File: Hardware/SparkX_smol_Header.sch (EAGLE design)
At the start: 31 parts, among them J1 QWIIC_RIGHT_ANGLE

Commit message: Update smôl logo
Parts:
- added U$39: SMOL_LOGOSMALL, SparkX:SMOL_LOGOSMALL
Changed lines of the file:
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@@
 <part name="LOGO3" library="SparkFun-Aesthetics" deviceset="OSHW-LOGO" device="MINI"/>
 <part name="LOGO4" library="SparkFun-Aesthetics" deviceset="QWIIC_LOGO" device="_5MM"/>
+<part name="U$39" library="SparkX" deviceset="SMOL_LOGO" device="SMALL"/>
 </parts>
 <sheets>
@@
 <instance part="LOGO3" gate="G$1" x="307.34" y="25.4" smashed="yes"/>
 <instance part="LOGO4" gate="G$1" x="307.34" y="38.1" smashed="yes"/>
+<instance part="U$39" gate="G$1" x="307.34" y="50.8" smashed="yes"/>
 </instances>
 <busses>

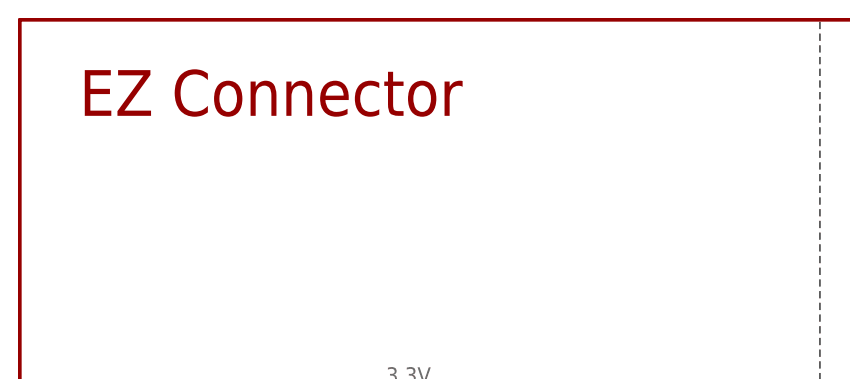
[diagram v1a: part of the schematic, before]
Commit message: Change EZ to smôl on schematic
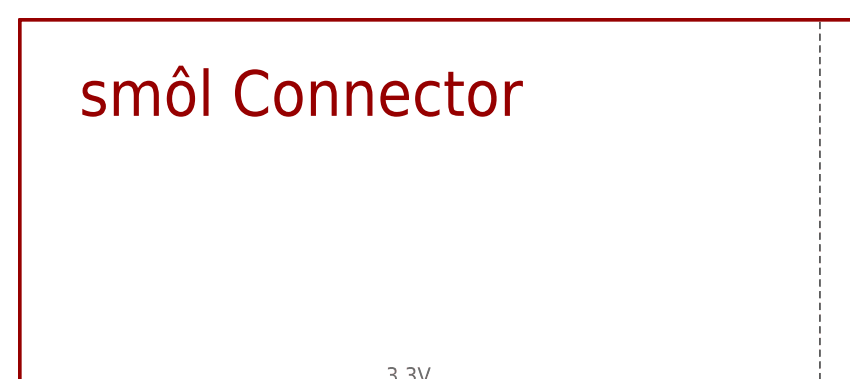
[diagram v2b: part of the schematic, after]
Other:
- note added: "smôl Connector"
- note removed: "EZ Connector"
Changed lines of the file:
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@@
 <wire x1="201.93" y1="160.02" x2="201.93" y2="279.4" width="0.2032" layer="97" style="longdash"/>
 <wire x1="88.9" y1="160.02" x2="0" y2="160.02" width="0.2032" layer="97" style="longdash"/>
-<text x="6.604" y="268.732" size="5.08" layer="94">EZ Connector</text>
+<text x="6.604" y="268.732" size="5.08" layer="94">smôl Connector</text>
 <text x="56.642" y="218.44" size="2.54" layer="97" font="vector" rot="R270">Top</text>
 <text x="96.774" y="268.732" size="5.08" layer="94">Header</text>
